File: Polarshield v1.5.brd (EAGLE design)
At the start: 100 x 80 mm, 60 parts, among them CN1 1X4-CLEANBIG, CN2 1X4-CLEANBIG, J1 1X2-3.5MM, U1 ARDUINO_MEGA_SHIELD, X1 2.1MMJACKTHM

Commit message: Added some LEDs for rx, tx and step
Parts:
- removed POWER: (no value), led:CHIP-LED0805
- removed R41: 1K, rcl:R0805
- added PWR, RX_LED, TX_LED, T_STP, X_STP, Y_STP: (no value), led:CHIP-LED0805
- added R3, R4, R6: 1K, rcl:R0805
- added RN6: 1K, resistor-dil:EXBS8V
- moved D13 8.07 mm to (27.9, 10.2)
- moved JP15 2.50 mm to (13.8, 71.2)
- moved SER1 2.50 mm to (4.99, 71.2)
- moved SER2 2.50 mm to (7.53, 71.2)
- moved R26 1.73 mm to (48.6, 77.5)
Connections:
- net T-DIR renamed X-DIR
- net T-EN renamed X-EN
- removed net T-STEP: CN1.4, U$6.STEP, U1.D31
- new net N$15: RN6.2, RX_LED.C
- new net N$16: RN6.3, TX_LED.C
- new net N$18: R4.1, Y_STP.A
- new net N$19: R6.1, X_STP.A
- new net N$23: R3.1, T_STP.A
- new net X-STEP: CN1.4, R3.2, U$6.STEP, U1.D31
- net D0: now also RN6.7
- net D1: now also RN6.6
- net GND: now also PWR.C, T_STP.C, X_STP.C, Y_STP.C; no longer POWER.C
- net N$2: now also PWR.A, RN6.4; no longer POWER.A, R41.1
- net VCC: now also RN6.5, RX_LED.A, TX_LED.A; no longer R41.2
- net Y-STEP: now also R4.2
- net Z-STEP: now also R6.2
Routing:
- net D1: track 2.59 -> 75.6 mm, vias 0 -> 7
- net X-STEP: track 0.00 -> 69.1 mm
- net T-STEP: track 69.1 -> 0.00 mm
- net D0: track 2.59 -> 58.8 mm, vias 0 -> 3
- net GND: track 512.1 -> 488.2 mm, vias 4 -> 5
- net +12V: track 123.7 -> 105.8 mm, vias 2 -> 1
- net LED: track 92.7 -> 77.8 mm
- net SERV1: track 85.9 -> 73.4 mm, vias 2 -> 3
- net N$6: track 40.2 -> 52.5 mm, vias 2 -> 0
- net N$2: track 7.73 -> 0.00 mm
- net +3V3: track 176.6 -> 171.8 mm, vias 3 -> 4
- net SERV2: track 68.0 -> 63.3 mm, vias 0 -> 1
- net VCC: track 286.3 -> 288.9 mm, vias 4 -> 5
- net RESET: track 19.0 -> 18.0 mm
- net TFT_LEDA: track 4.29 -> 5.08 mm
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
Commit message: Finished v1.5 and sent off to be made.
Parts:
- R3, R4, R6: value 1K -> 100
- moved R4 21.2 mm to (32.4, 17.5)
- moved Y_STP 4.85 mm to (18.3, 20.6), turned to 270 degrees
- moved X_STP 4.04 mm to (14.4, 59.6), turned to 90 degrees
- moved R6 3.54 mm to (14.4, 61.8), turned to 180 degrees
- moved C2 2.62 mm to (17.0, 42.9)
- moved R3 0.74 mm to (13.3, 48.6)
- moved T_STP 0.54 mm to (17.4, 48.6)
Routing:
- net SERV2: track 63.3 -> 243.5 mm, vias 1 -> 15
- net Z-STEP: track 21.4 -> 69.2 mm, vias 0 -> 3
- net X-STEP: track 69.1 -> 116.8 mm, vias 0 -> 3
- net GND: track 488.2 -> 519.0 mm, vias 5 -> 7
- net N$16: track 0.00 -> 24.0 mm, vias 0 -> 2
- net N$18: track 0.00 -> 19.6 mm, vias 0 -> 2
- net VCC: track 288.9 -> 304.7 mm
- net N$2: track 0.00 -> 14.9 mm, vias 0 -> 2
- net N$15: track 0.00 -> 10.9 mm
- net Y-STEP: track 44.7 -> 49.6 mm
- net LED: track 77.8 -> 80.9 mm, vias 3 -> 6
- net N$19: track 0.00 -> 3.02 mm
- net N$23: track 0.00 -> 2.22 mm
- net SPI_MOSI: track 99.1 -> 97.0 mm
- net SPI_SS: track 96.9 -> 96.3 mm
- added copper zone on layer 1, net GND
- added copper zone on layer 16, net GND
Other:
- board text added: "10K"

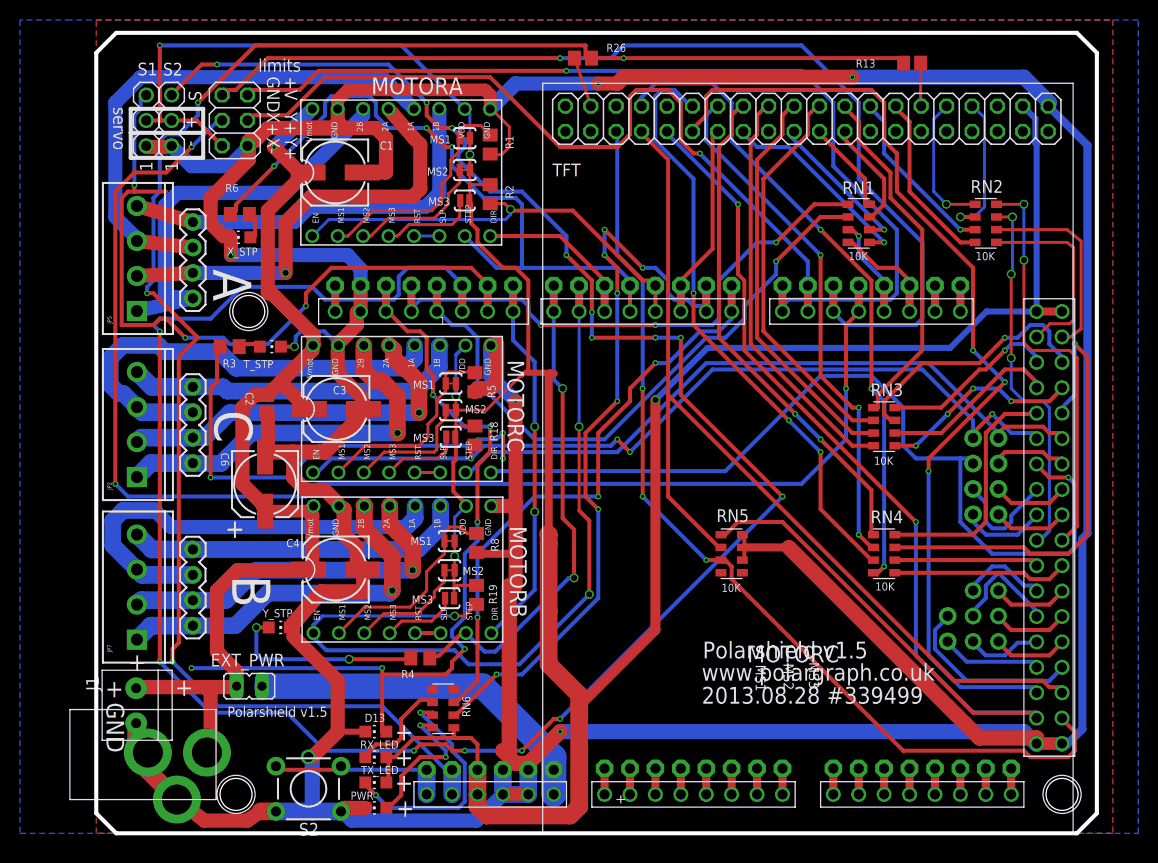
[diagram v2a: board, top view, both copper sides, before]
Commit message: Merged a resistor into a network and changed a few values, also cleaned up silkscreen.
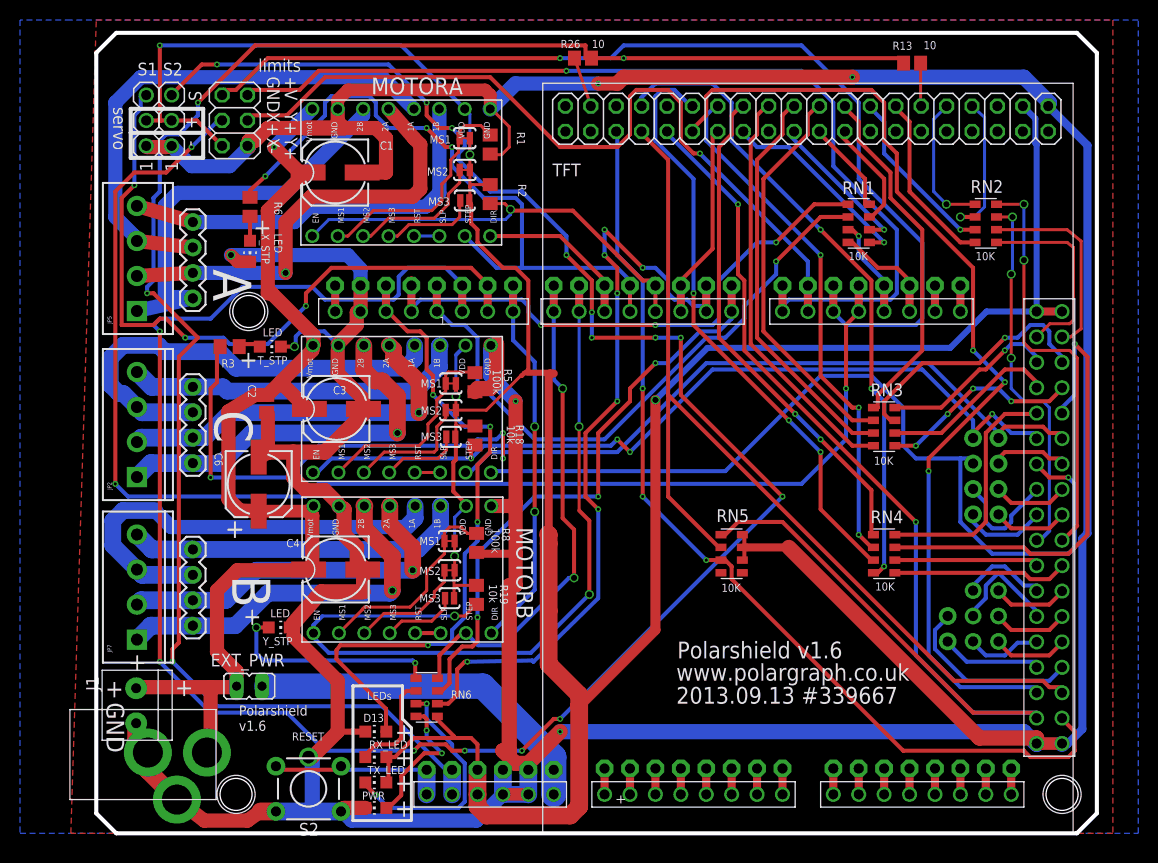
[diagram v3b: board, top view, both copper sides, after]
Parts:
- removed R4: 100, rcl:R0805
- R3: value 100 -> 1K
- R6: value 100 -> 1k
- moved RN6 2.01 mm to (33.0, 13.6)
- moved X_STP 1.73 mm to (15.4, 58.2), turned to 180 degrees
- moved R6 1.27 mm to (15.4, 62.6), turned to 90 degrees
- moved C6 0.63 mm to (16.2, 34.9)
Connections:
- net N$18: now also RN6.1; no longer R4.1
- net Y-STEP: now also RN6.8; no longer R4.2
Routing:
- net LED: track 80.9 -> 66.7 mm, vias 6 -> 4
- net GND: track 519.0 -> 508.3 mm
- net SERV1: track 73.4 -> 69.9 mm
- net +12V: track 105.4 -> 108.3 mm
- net D1: track 75.6 -> 78.3 mm
- net Z-STEP: track 69.2 -> 66.6 mm
- net N$18: track 19.6 -> 21.7 mm
- net VCC: track 304.7 -> 306.5 mm
- net Y-EN: track 81.2 -> 80.3 mm
- net Y-STEP: track 49.6 -> 50.4 mm
- net N$2: track 14.9 -> 14.2 mm
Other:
- board text added: "10"
- board text added: "100k"
- board text added: "10k"
- board text added: "2013.09.13 #339667"
- board text added: "LED"
- board text added: "LEDs"
- board text added: "Polarshield v1.6"
- board text added: "RESET"
- board text removed: "2013.08.28 #339499"
- board text removed: "MOTORC"
- board text removed: "Polarshield v1.5"
